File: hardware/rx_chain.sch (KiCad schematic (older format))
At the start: 19 parts

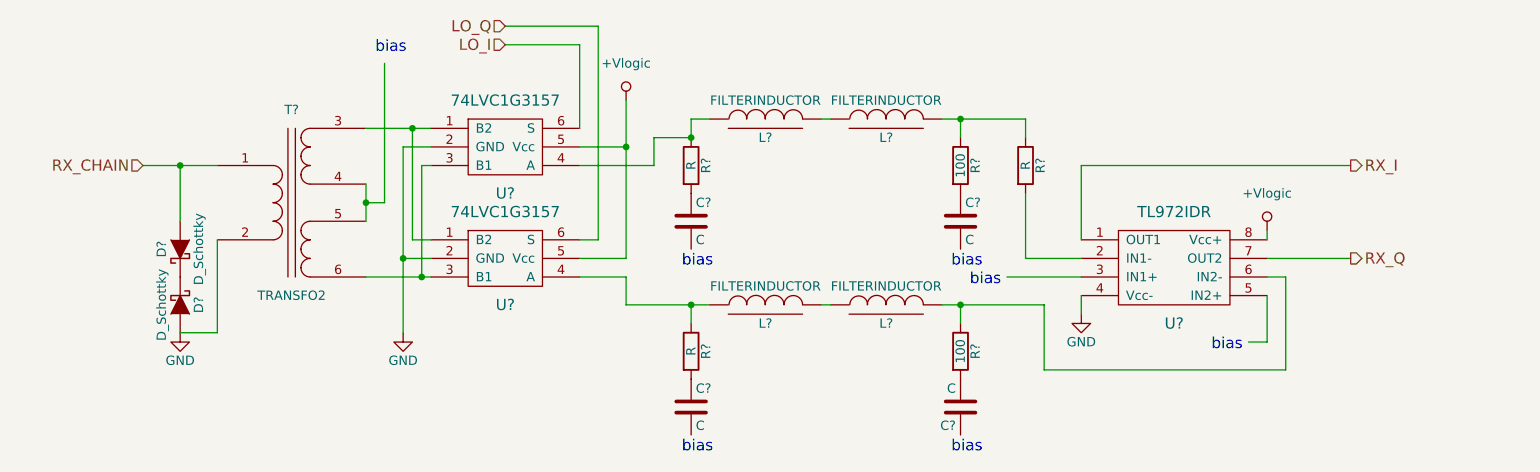
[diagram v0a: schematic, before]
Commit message: Added biases for RX and TX chains where needed
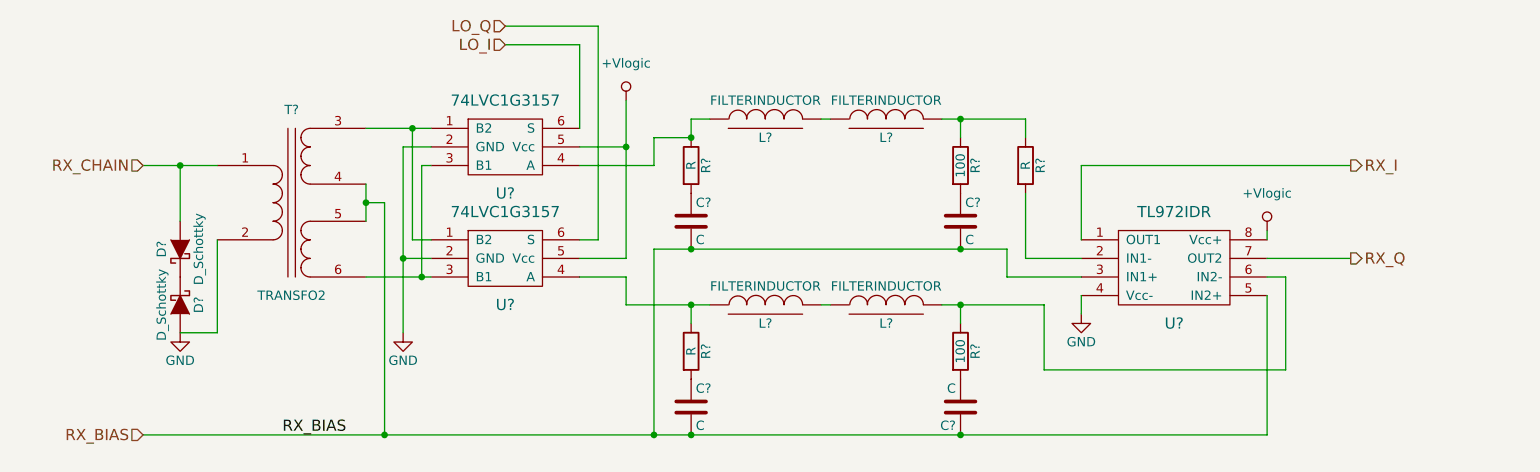
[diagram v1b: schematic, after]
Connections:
- net labels added: RX_BIAS
- wire segments 54 -> 57
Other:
- note removed: "bias"
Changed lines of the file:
@@
 Comp "PRK - OH2TI"
 Comment1 "exla - OH2EHK"
-Comment2 ""
+Comment2 "tejeez - OH2EAT"
 Comment3 ""
 Comment4 ""
@@
 	1    0    0    -1
 $EndComp
-Text Notes 2650 2300 0    60   ~ 0
-bias
 $Comp
 L +Vlogic #PWR036
@@
 	0    -1   -1   0
 $EndComp
-Wire Wire Line
-	1800 3300 1800 3800
-Wire Wire Line
-	1800 3800 1600 3800
-Wire Wire Line
-	1400 2900 1800 2900
-Wire Wire Line
-	1600 2900 1600 3200
-Connection ~ 1600 2900
-Wire Wire Line
-	2600 3000 2600 3200
-Wire Wire Line
-	2600 3500 2950 3500
-Wire Wire Line
-	2600 2700 2950 2700
-Wire Wire Line
-	2950 2800 2800 2800
-Wire Wire Line
-	2800 2800 2800 3800
-Wire Wire Line
-	2950 3400 2800 3400
-Connection ~ 2800 3400
-Wire Wire Line
-	2950 3300 2850 3300
-Wire Wire Line
-	2850 3300 2850 2700
-Connection ~ 2850 2700
-Wire Wire Line
-	2600 3100 2700 3100
-Wire Wire Line
-	2700 3100 2700 2350
-Connection ~ 2600 3100
-Wire Wire Line
-	2950 2900 2900 2900
-Wire Wire Line
-	2900 2900 2900 3500
-Connection ~ 2900 3500
-Wire Wire Line
-	3750 2800 4000 2800
-Wire Wire Line
-	4000 2550 4000 3400
-Wire Wire Line
-	4000 3400 3750 3400
-Connection ~ 4000 2800
-Wire Wire Line
-	3350 2250 3750 2250
-Wire Wire Line
-	3750 2250 3750 2700
-Wire Wire Line
-	3350 2150 3850 2150
-Wire Wire Line
-	3850 2150 3850 3300
-Wire Wire Line
-	3850 3300 3750 3300
-Wire Wire Line
-	4350 2750 4350 2650
-Connection ~ 4350 2750
-Wire Wire Line
-	5050 2650 5100 2650
-Wire Wire Line
-	5700 2650 6150 2650
 $Comp
 L FILTERINDUCTOR L?
@@
 	0    -1   -1   0
 $EndComp
-Wire Wire Line
-	5050 3650 5100 3650
-Wire Wire Line
-	4350 3750 4350 3650
-Wire Wire Line
-	4000 3650 4450 3650
-Wire Wire Line
-	5700 3650 6250 3650
-Wire Wire Line
-	5800 3650 5800 3750
-Wire Wire Line
-	5800 2650 5800 2750
-Wire Wire Line
-	4350 2650 4450 2650
-Wire Wire Line
-	3750 3500 4000 3500
-Wire Wire Line
-	4000 3500 4000 3650
-Connection ~ 4350 3650
-Wire Wire Line
-	3750 2900 4150 2900
-Wire Wire Line
-	4150 2900 4150 2750
-Wire Wire Line
-	4150 2750 4350 2750
-Text Notes 4300 3450 0    60   ~ 0
-bias
-Text Notes 5750 3450 0    60   ~ 0
-bias
-Text Notes 4300 4450 0    60   ~ 0
-bias
-Text Notes 5750 4450 0    60   ~ 0
-bias
 $Comp
 L TL972IDR U?
@@
 	1    0    0    -1
 $EndComp
-Wire Wire Line
-	7450 3250 7450 3300
 $Comp
 L R R?
@@
 	1    0    0    -1
 $EndComp
-Wire Wire Line
-	6150 2650 6150 2750
-Connection ~ 5800 2650
-Wire Wire Line
-	6150 3050 6150 3400
-Wire Wire Line
-	6150 3400 6450 3400
-Wire Wire Line
-	6450 3500 6050 3500
-Text Notes 5850 3550 0    60   ~ 0
-bias
 $Comp
 L GND #PWR038
@@
 	1    0    0    -1
 $EndComp
-Wire Wire Line
-	6450 3600 6450 3700
-Wire Wire Line
-	6250 3650 6250 4000
-Wire Wire Line
-	6250 4000 7550 4000
-Wire Wire Line
-	7550 4000 7550 3500
-Wire Wire Line
-	7550 3500 7450 3500
-Connection ~ 5800 3650
-Wire Wire Line
-	7450 3600 7450 3850
-Wire Wire Line
-	7450 3850 7350 3850
-Text Notes 7150 3900 0    60   ~ 0
-bias
 Text HLabel 7900 2900 2    60   Output ~ 0
 RX_I
 Text HLabel 7900 3400 2    60   Output ~ 0
 RX_Q
+Text HLabel 1400 4350 0    60   Input ~ 0
+RX_BIAS
+Wire Wire Line
+	1800 3300 1800 3800
+Wire Wire Line
+	1800 3800 1600 3800
+Wire Wire Line
+	1400 2900 1800 2900
+Wire Wire Line
+	1600 2900 1600 3200
+Connection ~ 1600 2900
+Wire Wire Line
+	2600 3000 2600 3200
+Wire Wire Line
+	2600 3500 2950 3500
+Wire Wire Line
+	2600 2700 2950 2700
+Wire Wire Line
+	2950 2800 2800 2800
+Wire Wire Line
+	2800 2800 2800 3800
+Wire Wire Line
+	2950 3400 2800 3400
+Connection ~ 2800 3400
+Wire Wire Line
+	2950 3300 2850 3300
+Wire Wire Line
+	2850 3300 2850 2700
+Connection ~ 2850 2700
+Wire Wire Line
+	2600 3100 2700 3100
+Wire Wire Line
+	2700 3100 2700 4350
+Connection ~ 2600 3100
+Wire Wire Line
+	2950 2900 2900 2900
+Wire Wire Line
+	2900 2900 2900 3500
+Connection ~ 2900 3500
+Wire Wire Line
+	3750 2800 4000 2800
+Wire Wire Line
+	4000 2550 4000 3400
+Wire Wire Line
+	4000 3400 3750 3400
+Connection ~ 4000 2800
+Wire Wire Line
+	3350 2250 3750 2250
+Wire Wire Line
+	3750 2250 3750 2700
+Wire Wire Line
+	3350 2150 3850 2150
+Wire Wire Line
+	3850 2150 3850 3300
+Wire Wire Line
+	3850 3300 3750 3300
+Wire Wire Line
+	4350 2750 4350 2650
+Connection ~ 4350 2750
+Wire Wire Line
+	5050 2650 5100 2650
+Wire Wire Line
+	5700 2650 6150 2650
+Wire Wire Line
+	5050 3650 5100 3650
+Wire Wire Line
+	4350 3750 4350 3650
+Wire Wire Line
+	4000 3650 4450 3650
+Wire Wire Line
+	5700 3650 6250 3650
+Wire Wire Line
+	5800 3650 5800 3750
+Wire Wire Line
+	5800 2650 5800 2750
+Wire Wire Line
+	4350 2650 4450 2650
+Wire Wire Line
+	3750 3500 4000 3500
+Wire Wire Line
+	4000 3500 4000 3650
+Connection ~ 4350 3650
+Wire Wire Line
+	3750 2900 4150 2900
+Wire Wire Line
+	4150 2900 4150 2750
+Wire Wire Line
+	4150 2750 4350 2750
+Wire Wire Line
+	7450 3250 7450 3300
+Wire Wire Line
+	6150 2650 6150 2750
+Connection ~ 5800 2650
+Wire Wire Line
+	6150 3050 6150 3400
+Wire Wire Line
+	6150 3400 6450 3400
+Wire Wire Line
+	6450 3500 6050 3500
+Wire Wire Line
+	6450 3600 6450 3700
+Wire Wire Line
+	6250 3650 6250 4000
+Wire Wire Line
+	6250 4000 7550 4000
+Wire Wire Line
+	7550 4000 7550 3500
+Wire Wire Line
+	7550 3500 7450 3500
+Connection ~ 5800 3650
+Wire Wire Line
+	7450 4350 7450 3600
 Wire Wire Line
 	6450 3300 6450 2900
@@
 Wire Wire Line
 	7450 3400 7900 3400
+Wire Wire Line
+	1400 4350 7450 4350
+Connection ~ 5800 4350
+Connection ~ 2700 4350
+Connection ~ 4350 4350
+Text Label 2150 4350 0    60   ~ 0
+RX_BIAS
+Wire Wire Line
+	6050 3350 6050 3500
+Wire Wire Line
+	4150 3350 6050 3350
+Connection ~ 5800 3350
+Wire Wire Line
+	4150 3350 4150 4350
+Connection ~ 4150 4350
+Connection ~ 4350 3350
 $EndSCHEMATC

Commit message: Made some minor adjustments and replotted schematic .pdf
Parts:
- removed D? (x2): D_Schottky, symbol D_Schottky
- added D? (x2): ZENER, symbol ZENER
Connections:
- net GND: now also D?.2 (A)
- net RX_CHAIN: now also D?.2 (A)
- new net: D?.1 (K), D?.1 (K)
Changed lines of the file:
@@
 Comment4 ""
 $EndDescr
-Text HLabel 1400 2900 0    60   Input ~ 0
+Text HLabel 1300 2600 0    60   Input ~ 0
 RX_CHAIN
-$Comp
-L D_Schottky D?
-U 1 1 57E45095
-P 1600 3350
-F 0 "D?" H 1600 3450 50  0000 C CNN
-F 1 "D_Schottky" H 1600 3250 50  0000 C CNN
-F 2 "" H 1600 3350 50  0000 C CNN
-F 3 "" H 1600 3350 50  0000 C CNN
-	1    1600 3350
-	0    -1   -1   0
-$EndComp
-$Comp
-L D_Schottky D?
-U 1 1 57E45103
-P 1600 3650
-F 0 "D?" H 1600 3750 50  0000 C CNN
-F 1 "D_Schottky" H 1600 3550 50  0000 C CNN
-F 2 "" H 1600 3650 50  0000 C CNN
-F 3 "" H 1600 3650 50  0000 C CNN
-	1    1600 3650
-	0    1    1    0
-$EndComp
 $Comp
 L GND #PWR034
 U 1 1 57E45141
-P 1600 3800
-F 0 "#PWR034" H 1600 3550 50  0001 C CNN
-F 1 "GND" H 1600 3650 50  0000 C CNN
-F 2 "" H 1600 3800 50  0000 C CNN
-F 3 "" H 1600 3800 50  0000 C CNN
-	1    1600 3800
+P 1600 3600
+F 0 "#PWR034" H 1600 3350 50  0001 C CNN
+F 1 "GND" H 1600 3450 50  0000 C CNN
+F 2 "" H 1600 3600 50  0000 C CNN
+F 3 "" H 1600 3600 50  0000 C CNN
+	1    1600 3600
 	1    0    0    -1
 $EndComp
@@
 RX_BIAS
 Wire Wire Line
-	1800 3300 1800 3800
-Wire Wire Line
-	1800 3800 1600 3800
-Wire Wire Line
-	1400 2900 1800 2900
-Wire Wire Line
-	1600 2900 1600 3200
-Connection ~ 1600 2900
-Wire Wire Line
-	2600 3000 2600 3200
-Wire Wire Line
-	2600 3500 2950 3500
-Wire Wire Line
-	2600 2700 2950 2700
+	1800 3300 1800 3600
+Wire Wire Line
+	1800 3600 1600 3600
+Wire Wire Line
+	1600 2600 1600 2700
+Wire Wire Line
+	2600 3000 2600 3100
+Wire Wire Line
+	2600 3100 2600 3200
+Wire Wire Line
+	2600 3500 2900 3500
+Wire Wire Line
+	2900 3500 2950 3500
+Wire Wire Line
+	2600 2700 2850 2700
+Wire Wire Line
+	2850 2700 2950 2700
 Wire Wire Line
 	2950 2800 2800 2800
 Wire Wire Line
-	2800 2800 2800 3800
+	2800 2800 2800 3400
+Wire Wire Line
+	2800 3400 2800 3800
 Wire Wire Line
 	2950 3400 2800 3400
@@
 	3750 2800 4000 2800
 Wire Wire Line
-	4000 2550 4000 3400
+	4000 2550 4000 2800
+Wire Wire Line
+	4000 2800 4000 3400
 Wire Wire Line
 	4000 3400 3750 3400
@@
 	5050 2650 5100 2650
 Wire Wire Line
-	5700 2650 6150 2650
+	5700 2650 5800 2650
+Wire Wire Line
+	5800 2650 6150 2650
 Wire Wire Line
 	5050 3650 5100 3650
@@
 	4350 3750 4350 3650
 Wire Wire Line
-	4000 3650 4450 3650
-Wire Wire Line
-	5700 3650 6250 3650
+	4000 3650 4350 3650
+Wire Wire Line
+	4350 3650 4450 3650
+Wire Wire Line
+	5700 3650 5800 3650
+Wire Wire Line
+	5800 3650 6250 3650
 Wire Wire Line
 	5800 3650 5800 3750
@@
 	7450 3400 7900 3400
 Wire Wire Line
-	1400 4350 7450 4350
+	1400 4350 2700 4350
+Wire Wire Line
+	2700 4350 4150 4350
+Wire Wire Line
+	4150 4350 4350 4350
+Wire Wire Line
+	4350 4350 5800 4350
+Wire Wire Line
+	5800 4350 7450 4350
 Connection ~ 5800 4350
 Connection ~ 2700 4350
@@
 	6050 3350 6050 3500
 Wire Wire Line
-	4150 3350 6050 3350
+	4150 3350 4350 3350
+Wire Wire Line
+	4350 3350 5800 3350
+Wire Wire Line
+	5800 3350 6050 3350
 Connection ~ 5800 3350
 Wire Wire Line
@@
 Connection ~ 4150 4350
 Connection ~ 4350 3350
+$Comp
+L ZENER D?
+U 1 1 57ED018F
+P 1600 3300
+F 0 "D?" H 1600 3400 50  0000 C CNN
+F 1 "ZENER" H 1600 3200 50  0000 C CNN
+F 2 "" H 1600 3300 50  0000 C CNN
+F 3 "" H 1600 3300 50  0000 C CNN
+	1    1600 3300
+	0    1    1    0
+$EndComp
+$Comp
+L ZENER D?
+U 1 1 57ED027D
+P 1600 2900
+F 0 "D?" H 1600 3000 50  0000 C CNN
+F 1 "ZENER" H 1600 2800 50  0000 C CNN
+F 2 "" H 1600 2900 50  0000 C CNN
+F 3 "" H 1600 2900 50  0000 C CNN
+	1    1600 2900
+	0    -1   -1   0
+$EndComp
+Wire Wire Line
+	1600 3600 1600 3500
+Wire Wire Line
+	1800 2600 1800 2900
+Wire Wire Line
+	1300 2600 1600 2600
+Wire Wire Line
+	1600 2600 1800 2600
+Connection ~ 1600 2600
 $EndSCHEMATC

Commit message: fixed some bugs
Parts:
- removed R? (x2): 100, symbol R
- added C?: 100nF, symbol C
- added C? (x2): 100pF, symbol C
- added R?: 100R, symbol R
- added R? (x2): 33k, symbol R
- L? (x4): value FILTERINDUCTOR -> 440µH
- R? (x3): value R -> 100R
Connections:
- net GND: now also C?.2
- net RX_BIAS: now also C?.1
- net RX_I: now also C?.2, R?.1
- net RX_Q: now also C?.1, R?.1
- net at C?.2: now also L?.2, R?.2
- net at U?.6 (IN2-): now also C?.2, R?.1, R?.2; no longer L?.2
- net at L?.2, R?.1: now also C?.1
- net at R?.2, U?.2 (IN1-): now also C?.1, R?.2
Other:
- moved on the sheet: C?, U?

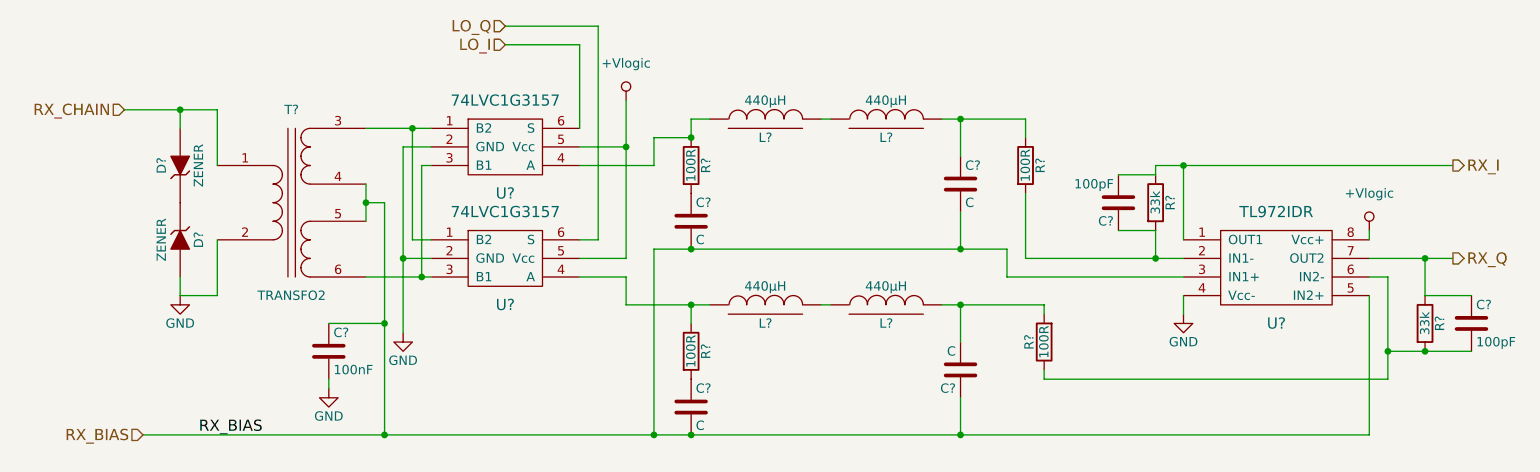
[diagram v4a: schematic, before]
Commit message: Added annotation so willing prove readers can reference components more easily
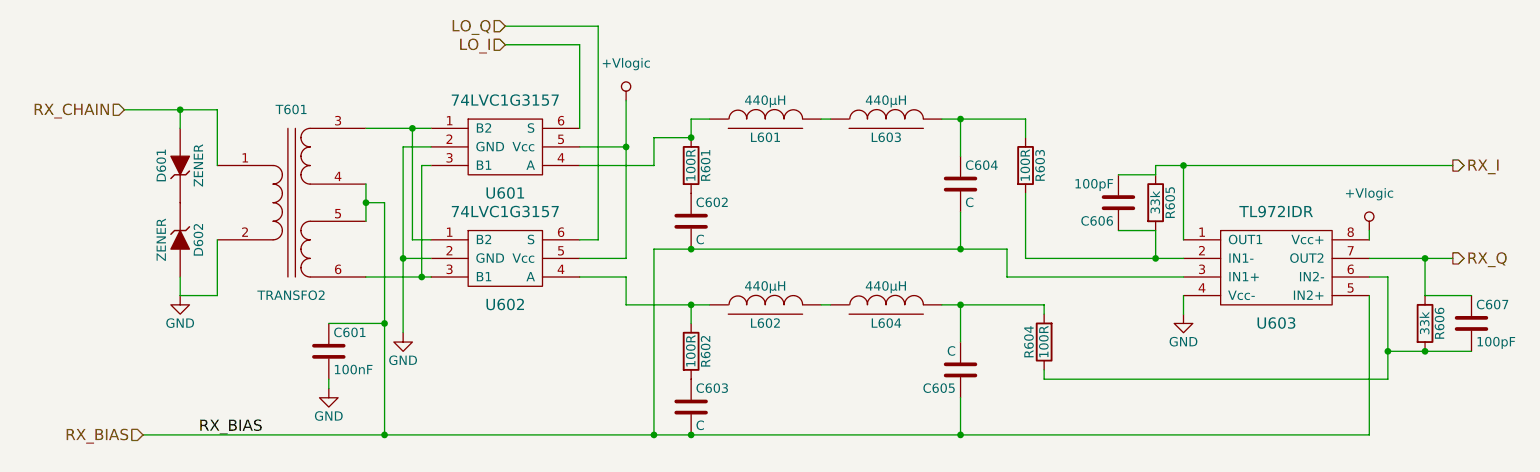
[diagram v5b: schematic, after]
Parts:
- gave numbers to parts that had none: 23
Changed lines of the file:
@@
 RX_CHAIN
 $Comp
-L GND #PWR034
+L GND #PWR601
 U 1 1 57E45141
 P 1600 3600
-F 0 "#PWR034" H 1600 3350 50  0001 C CNN
+F 0 "#PWR601" H 1600 3350 50  0001 C CNN
 F 1 "GND" H 1600 3450 50  0000 C CNN
 F 2 "" H 1600 3600 50  0000 C CNN
@@
 $EndComp
 $Comp
-L TRANSFO2 T?
+L TRANSFO2 T601
 U 1 1 57E45159
 P 2200 3100
-F 0 "T?" H 2200 3600 50  0000 C CNN
+F 0 "T601" H 2200 3600 50  0000 C CNN
 F 1 "TRANSFO2" H 2200 2600 50  0000 C CNN
 F 2 "" H 2200 3100 50  0000 C CNN
@@
 $EndComp
 $Comp
-L 74LVC1G3157 U?
+L 74LVC1G3157 U601
 U 1 1 57E45213
 P 3350 2800
-F 0 "U?" H 3350 2550 60  0000 C CNN
+F 0 "U601" H 3350 2550 60  0000 C CNN
 F 1 "74LVC1G3157" H 3350 3050 60  0000 C CNN
 F 2 "" H 3350 2700 60  0001 C CNN
@@
 $EndComp
 $Comp
-L 74LVC1G3157 U?
+L 74LVC1G3157 U602
 U 1 1 57E4524A
 P 3350 3400
-F 0 "U?" H 3350 3150 60  0000 C CNN
+F 0 "U602" H 3350 3150 60  0000 C CNN
 F 1 "74LVC1G3157" H 3350 3650 60  0000 C CNN
 F 2 "" H 3350 3300 60  0001 C CNN
@@
 $EndComp
 $Comp
-L GND #PWR035
+L GND #PWR603
 U 1 1 57E45302
 P 2800 3800
-F 0 "#PWR035" H 2800 3550 50  0001 C CNN
+F 0 "#PWR603" H 2800 3550 50  0001 C CNN
 F 1 "GND" H 2800 3650 50  0000 C CNN
 F 2 "" H 2800 3800 50  0000 C CNN
@@
 $EndComp
 $Comp
-L +Vlogic #PWR036
+L +Vlogic #PWR604
 U 1 1 57E45597
 P 4000 2550
-F 0 "#PWR036" H 4000 2350 50  0001 C CNN
+F 0 "#PWR604" H 4000 2350 50  0001 C CNN
 F 1 "+Vlogic" H 4000 2750 50  0000 C CNN
 F 2 "" H 4000 2550 50  0000 C CNN
@@
 LO_Q
 $Comp
-L R R?
+L R R601
 U 1 1 57E45986
 P 4350 2900
-F 0 "R?" V 4430 2900 50  0000 C CNN
+F 0 "R601" V 4430 2900 50  0000 C CNN
 F 1 "100R" V 4350 2900 50  0000 C CNN
 F 2 "" V 4280 2900 50  0000 C CNN
@@
 $EndComp
 $Comp
-L R R?
+L R R602
 U 1 1 57E459C1
 P 4350 3900
-F 0 "R?" V 4430 3900 50  0000 C CNN
+F 0 "R602" V 4430 3900 50  0000 C CNN
 F 1 "100R" V 4350 3900 50  0000 C CNN
 F 2 "" V 4280 3900 50  0000 C CNN
@@
 $EndComp
 $Comp
-L C C?
+L C C602
 U 1 1 57E45A29
 P 4350 3200
-F 0 "C?" H 4375 3300 50  0000 L CNN
+F 0 "C602" H 4375 3300 50  0000 L CNN
 F 1 "C" H 4375 3100 50  0000 L CNN
 F 2 "" H 4388 3050 50  0000 C CNN
@@
 $EndComp
 $Comp
-L C C?
+L C C603
 U 1 1 57E45A80
 P 4350 4200
-F 0 "C?" H 4375 4300 50  0000 L CNN
+F 0 "C603" H 4375 4300 50  0000 L CNN
 F 1 "C" H 4375 4100 50  0000 L CNN
 F 2 "" H 4388 4050 50  0000 C CNN
@@
 $EndComp
 $Comp
-L C C?
+L C C605
 U 1 1 57E45ACF
 P 5800 4000
-F 0 "C?" H 5825 4100 50  0000 L CNN
+F 0 "C605" H 5825 4100 50  0000 L CNN
 F 1 "C" H 5825 3900 50  0000 L CNN
 F 2 "" H 5838 3850 50  0000 C CNN
@@
 $EndComp
 $Comp
-L C C?
+L C C604
 U 1 1 57E45BC5
 P 5800 3000
-F 0 "C?" H 5825 3100 50  0000 L CNN
+F 0 "C604" H 5825 3100 50  0000 L CNN
 F 1 "C" H 5825 2900 50  0000 L CNN
 F 2 "" H 5838 2850 50  0000 C CNN
@@
 $EndComp
 $Comp
-L FILTERINDUCTOR L?
+L FILTERINDUCTOR L601
 U 1 1 57E45F48
 P 4750 2650
-F 0 "L?" V 4650 2650 50  0000 C CNN
+F 0 "L601" V 4650 2650 50  0000 C CNN
 F 1 "440µH" V 4850 2650 50  0000 C CNN
 F 2 "" H 4750 2650 50  0000 C CNN
@@
 $EndComp
 $Comp
-L FILTERINDUCTOR L?
+L FILTERINDUCTOR L603
 U 1 1 57E45FC9
 P 5400 2650
-F 0 "L?" V 5300 2650 50  0000 C CNN
+F 0 "L603" V 5300 2650 50  0000 C CNN
 F 1 "440µH" V 5500 2650 50  0000 C CNN
 F 2 "" H 5400 2650 50  0000 C CNN
@@
 $EndComp
 $Comp
-L FILTERINDUCTOR L?
+L FILTERINDUCTOR L602
 U 1 1 57E47294
 P 4750 3650
-F 0 "L?" V 4650 3650 50  0000 C CNN
+F 0 "L602" V 4650 3650 50  0000 C CNN
 F 1 "440µH" V 4850 3650 50  0000 C CNN
 F 2 "" H 4750 3650 50  0000 C CNN
@@
 $EndComp
 $Comp
-L FILTERINDUCTOR L?
+L FILTERINDUCTOR L604
 U 1 1 57E47303
 P 5400 3650
-F 0 "L?" V 5300 3650 50  0000 C CNN
+F 0 "L604" V 5300 3650 50  0000 C CNN
 F 1 "440µH" V 5500 3650 50  0000 C CNN
 F 2 "" H 5400 3650 50  0000 C CNN
@@
 $EndComp
 $Comp
-L TL972IDR U?
+L TL972IDR U603
 U 1 1 57E48699
 P 7500 3450
-F 0 "U?" H 7500 3150 60  0000 C CNN
+F 0 "U603" H 7500 3150 60  0000 C CNN
 F 1 "TL972IDR" H 7500 3750 60  0000 C CNN
 F 2 "" H 7550 3450 60  0001 C CNN
@@
 $EndComp
 $Comp
-L +Vlogic #PWR037
+L +Vlogic #PWR606
 U 1 1 57E48734
 P 8000 3250
-F 0 "#PWR037" H 8000 3050 50  0001 C CNN
+F 0 "#PWR606" H 8000 3050 50  0001 C CNN
 F 1 "+Vlogic" H 8000 3450 50  0000 C CNN
 F 2 "" H 8000 3250 50  0000 C CNN
@@
 $EndComp
 $Comp
-L R R?
+L R R603
 U 1 1 57E487DB
 P 6150 2900
-F 0 "R?" V 6230 2900 50  0000 C CNN
+F 0 "R603" V 6230 2900 50  0000 C CNN
 F 1 "100R" V 6150 2900 50  0000 C CNN
 F 2 "" V 6080 2900 50  0000 C CNN
@@
 $EndComp
 $Comp
-L GND #PWR038
+L GND #PWR605
 U 1 1 57E4894A
 P 7000 3700
-F 0 "#PWR038" H 7000 3450 50  0001 C CNN
+F 0 "#PWR605" H 7000 3450 50  0001 C CNN
 F 1 "GND" H 7000 3550 50  0000 C CNN
 F 2 "" H 7000 3700 50  0000 C CNN
@@
 Connection ~ 4350 3350
 $Comp
-L ZENER D?
+L ZENER D602
 U 1 1 57ED018F
 P 1600 3300
-F 0 "D?" H 1600 3400 50  0000 C CNN
+F 0 "D602" H 1600 3400 50  0000 C CNN
 F 1 "ZENER" H 1600 3200 50  0000 C CNN
 F 2 "" H 1600 3300 50  0000 C CNN
@@
 $EndComp
 $Comp
-L ZENER D?
+L ZENER D601
 U 1 1 57ED027D
 P 1600 2900
-F 0 "D?" H 1600 3000 50  0000 C CNN
+F 0 "D601" H 1600 3000 50  0000 C CNN
 F 1 "ZENER" H 1600 2800 50  0000 C CNN
 F 2 "" H 1600 2900 50  0000 C CNN
@@
 Connection ~ 1600 2600
 $Comp
-L R R?
+L R R604
 U 1 1 57EAD8F4
 P 6250 3850
-F 0 "R?" V 6330 3850 50  0000 C CNN
+F 0 "R604" V 6330 3850 50  0000 C CNN
 F 1 "100R" V 6250 3850 50  0000 C CNN
 F 2 "" V 6180 3850 50  0000 C CNN
@@
 	5800 4150 5800 4350
 $Comp
-L C C?
+L C C601
 U 1 1 57EAE0D5
 P 2400 3900
-F 0 "C?" H 2425 4000 50  0000 L CNN
+F 0 "C601" H 2425 4000 50  0000 L CNN
 F 1 "100nF" H 2425 3800 50  0000 L CNN
 F 2 "" H 2438 3750 50  0000 C CNN
@@
 $EndComp
 $Comp
-L GND #PWR?
+L GND #PWR602
 U 1 1 57EAE15A
 P 2400 4100
-F 0 "#PWR?" H 2400 3850 50  0001 C CNN
+F 0 "#PWR602" H 2400 3850 50  0001 C CNN
 F 1 "GND" H 2400 3950 50  0000 C CNN
 F 2 "" H 2400 4100 50  0000 C CNN
@@
 Connection ~ 2700 3750
 $Comp
-L C C?
+L C C606
 U 1 1 57EAE85D
 P 6650 3100
-F 0 "C?" H 6675 3200 50  0000 L CNN
+F 0 "C606" H 6675 3200 50  0000 L CNN
 F 1 "100pF" H 6675 3000 50  0000 L CNN
 F 2 "" H 6688 2950 50  0000 C CNN
@@
 $EndComp
 $Comp
-L C C?
+L C C607
 U 1 1 57EAE8CC
 P 8550 3750
-F 0 "C?" H 8575 3850 50  0000 L CNN
+F 0 "C607" H 8575 3850 50  0000 L CNN
 F 1 "100pF" H 8575 3650 50  0000 L CNN
 F 2 "" H 8588 3600 50  0000 C CNN
@@
 $EndComp
 $Comp
-L R R?
+L R R605
 U 1 1 57EAE910
 P 6850 3100
-F 0 "R?" V 6930 3100 50  0000 C CNN
+F 0 "R605" V 6930 3100 50  0000 C CNN
 F 1 "33k" V 6850 3100 50  0000 C CNN
 F 2 "" V 6780 3100 50  0000 C CNN
@@
 $EndComp
 $Comp
-L R R?
+L R R606
 U 1 1 57EAE9F7
 P 8300 3750
-F 0 "R?" V 8380 3750 50  0000 C CNN
+F 0 "R606" V 8380 3750 50  0000 C CNN
 F 1 "33k" V 8300 3750 50  0000 C CNN
 F 2 "" V 8230 3750 50  0000 C CNN
